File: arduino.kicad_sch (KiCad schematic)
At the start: 10 parts, among them J10 Conn_01x01_Female, J11 Conn_01x03_Male, J12 Conn_01x01_Female, J13 Conn_01x01_Female, J14 Conn_01x03_Male, J15 Conn_01x01_Female, J16 Conn_01x01_Female, J17 Conn_01x03_Male, J18 Conn_01x01_Female, U9 CD74HC4067SM

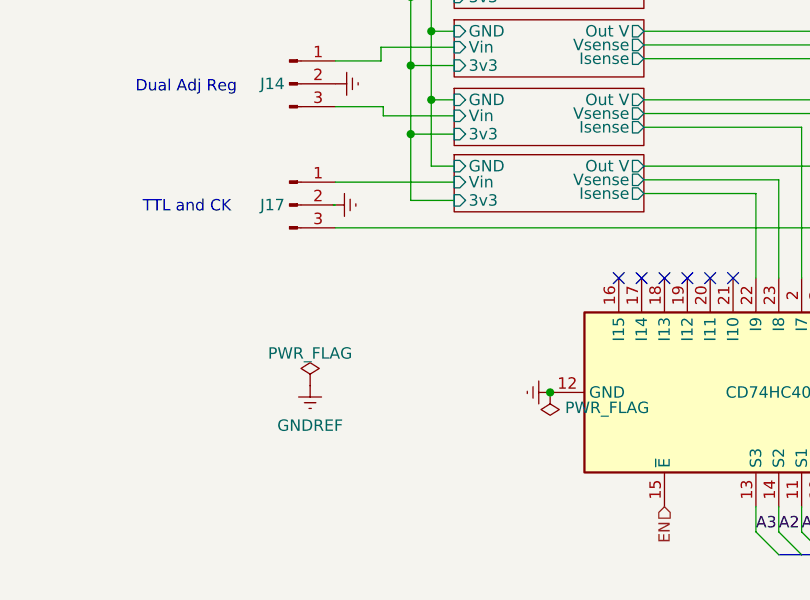
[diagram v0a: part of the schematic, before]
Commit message: sorting out earths and making measure mux board
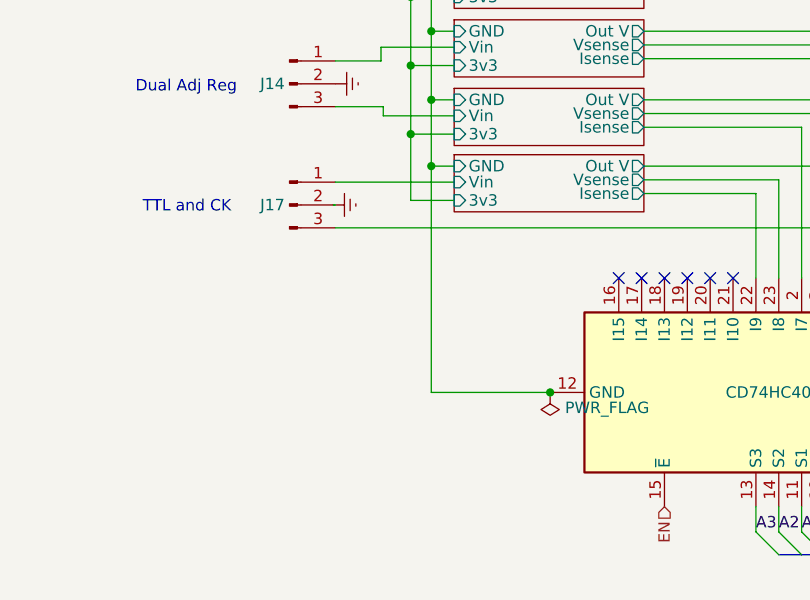
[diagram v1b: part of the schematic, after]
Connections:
- net Earth: no longer U9.12 (GND)
- net GND: now also U9.12 (GND)
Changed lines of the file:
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@@
   (junction (at 114.808 77.47) (diameter 0) (color 0 0 0 0)
   )
+  (junction (at 128.016 117.602) (diameter 0) (color 0 0 0 0)
+  )
   (junction (at 106.934 70.358) (diameter 0) (color 0 0 0 0)
   )
+  (junction (at 114.808 92.456) (diameter 0) (color 0 0 0 0)
+  )
   (junction (at 114.808 62.23) (diameter 0) (color 0 0 0 0)
   )
@@
   )
   (junction (at 112.522 81.28) (diameter 0) (color 0 0 0 0)
-  )
-  (junction (at 128.016 117.602) (diameter 0) (color 0 0 0 0)
   )
   (junction (at 108.966 64.008) (diameter 0) (color 0 0 0 0)
@@
     (stroke (width 0) (type default) (color 0 0 0 0))
   )
+  (wire (pts (xy 114.808 92.456) (xy 114.808 117.602))
+    (stroke (width 0) (type default) (color 0 0 0 0))
+  )
   (wire (pts (xy 138.43 80.518) (xy 161.036 80.518))
     (stroke (width 0) (type default) (color 0 0 0 0))
@@
   )
   (bus (pts (xy 158.496 135.636) (xy 161.036 135.636))
+    (stroke (width 0) (type default) (color 0 0 0 0))
+  )
+  (wire (pts (xy 114.808 117.602) (xy 128.016 117.602))
     (stroke (width 0) (type default) (color 0 0 0 0))
   )
@@
     (pin "1")
   )
-  (symbol (lib_id "power:GNDREF") (at 101.346 116.84 0) (unit 1)
-    (in_bom yes) (on_board yes) (fields_autoplaced)
-    (property "Reference" "#PWR0104" (id 0) (at 101.346 123.19 0)
-      (effects (font (size 1.27 1.27)) hide)
-    )
-    (property "Value" "GNDREF" (id 1) (at 101.346 121.2834 0))
-    (property "Footprint" "" (id 2) (at 101.346 116.84 0)
-      (effects (font (size 1.27 1.27)) hide)
-    )
-    (property "Datasheet" "" (id 3) (at 101.346 116.84 0)
-      (effects (font (size 1.27 1.27)) hide)
-    )
-    (pin "1")
-  )
   (symbol (lib_id "Connector:Conn_01x01_Female") (at 203.2 85.09 0) (unit 1)
     (in_bom yes) (on_board yes) (fields_autoplaced)
@@
     (pin "2")
     (pin "3")
-  )
-  (symbol (lib_id "power:PWR_FLAG") (at 101.346 116.84 0) (unit 1)
-    (in_bom yes) (on_board yes) (fields_autoplaced)
-    (property "Reference" "#FLG0117" (id 0) (at 101.346 114.935 0)
-      (effects (font (size 1.27 1.27)) hide)
-    )
-    (property "Value" "PWR_FLAG" (id 1) (at 101.346 113.2642 0))
-    (property "Footprint" "" (id 2) (at 101.346 116.84 0)
-      (effects (font (size 1.27 1.27)) hide)
-    )
-    (property "Datasheet" "~" (id 3) (at 101.346 116.84 0)
-      (effects (font (size 1.27 1.27)) hide)
-    )
-    (pin "1")
   )
   (symbol (lib_id "Connector:Conn_01x01_Female") (at 203.2 92.456 0) (unit 1)
@@
       (effects (font (size 1.27 1.27)) hide)
     )
-    (pin "1")
-  )
-  (symbol (lib_id "power:Earth") (at 128.016 117.602 270) (unit 1)
-    (in_bom no) (on_board yes) (fields_autoplaced)
-    (property "Reference" "#PWR07" (id 0) (at 121.666 117.602 0)
-      (effects (font (size 1.27 1.27)) hide)
-    )
-    (property "Value" "Earth" (id 1) (at 124.206 117.602 0)
-      (effects (font (size 1.27 1.27)) hide)
-    )
-    (property "Footprint" "" (id 2) (at 128.016 117.602 0)
-      (effects (font (size 1.27 1.27)) hide)
-    )
-    (property "Datasheet" "~" (id 3) (at 128.016 117.602 0)
-      (effects (font (size 1.27 1.27)) hide)
-    )

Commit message: last TH mounting board
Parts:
- added C10, C11, C12, C13, C14, C15, C16, C17: 0.1uF, Capacitor_SMD:C_0603_1608Metric, symbol Device:C_Small
- J1: renamed from J10; footprint (none) -> Connector_PinHeader_2.54mm:PinHeader_1x01_P2.54mm_Vertical
- J2: renamed from J11; footprint (none) -> Connector_PinHeader_2.54mm:PinHeader_1x03_P2.54mm_Horizontal
- J3: renamed from J12; footprint (none) -> Connector_PinHeader_2.54mm:PinHeader_1x01_P2.54mm_Vertical
- J4: renamed from J13; footprint (none) -> Connector_PinHeader_2.54mm:PinHeader_1x01_P2.54mm_Vertical
- J5: renamed from J14; footprint (none) -> Connector_PinHeader_2.54mm:PinHeader_1x03_P2.54mm_Horizontal
- J6: renamed from J15; footprint (none) -> Connector_PinHeader_2.54mm:PinHeader_1x01_P2.54mm_Vertical
- J7: renamed from J16; footprint (none) -> Connector_PinHeader_2.54mm:PinHeader_1x01_P2.54mm_Vertical
- J8: renamed from J17; footprint (none) -> Connector_PinHeader_2.54mm:PinHeader_1x03_P2.54mm_Horizontal
- J9: renamed from J18; footprint (none) -> Connector_PinHeader_2.54mm:PinHeader_1x01_P2.54mm_Vertical
- renumbered U9 to U4
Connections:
- net Earth is gone; now on net GND: J2.2 (Pin_2), J5.2 (Pin_2), J8.2 (Pin_2)
- net Curent and Volt4/Out V: now also C12.2
- net Curent and Volt5/Out V: now also C13.2
- net Curent and Volt5/Vsense: no longer U4.7 (I2)
- net Curent and Volt6/Out V: now also C14.2
- net Curent and Volt7/Out V: now also C15.2
- net Curent and Volt7/Vsense: no longer U4.3 (I6)
- net Curent and Volt8/Out V: now also C16.2
- net GND: now also C10.1, C11.1, C12.1, C13.1, C14.1, C15.1, C16.1, C17.1
- net Vunreg+: now also C11.2
- net Vunreg-: now also C10.2
- net at J8.3 (Pin_3), J9.1 (Pin_1): now also C17.2
- new net Unity Inverter/Ainv: U4.7 (I2)
- new net Unity Inverter1/Ainv: U4.3 (I6)
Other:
- added sheet Unity Inverter (UnityInverter.kicad_sch)
- added sheet Unity Inverter1 (UnityInverter.kicad_sch)
- moved on the sheet: J1, J3, J4, J6, J7, J9, U4

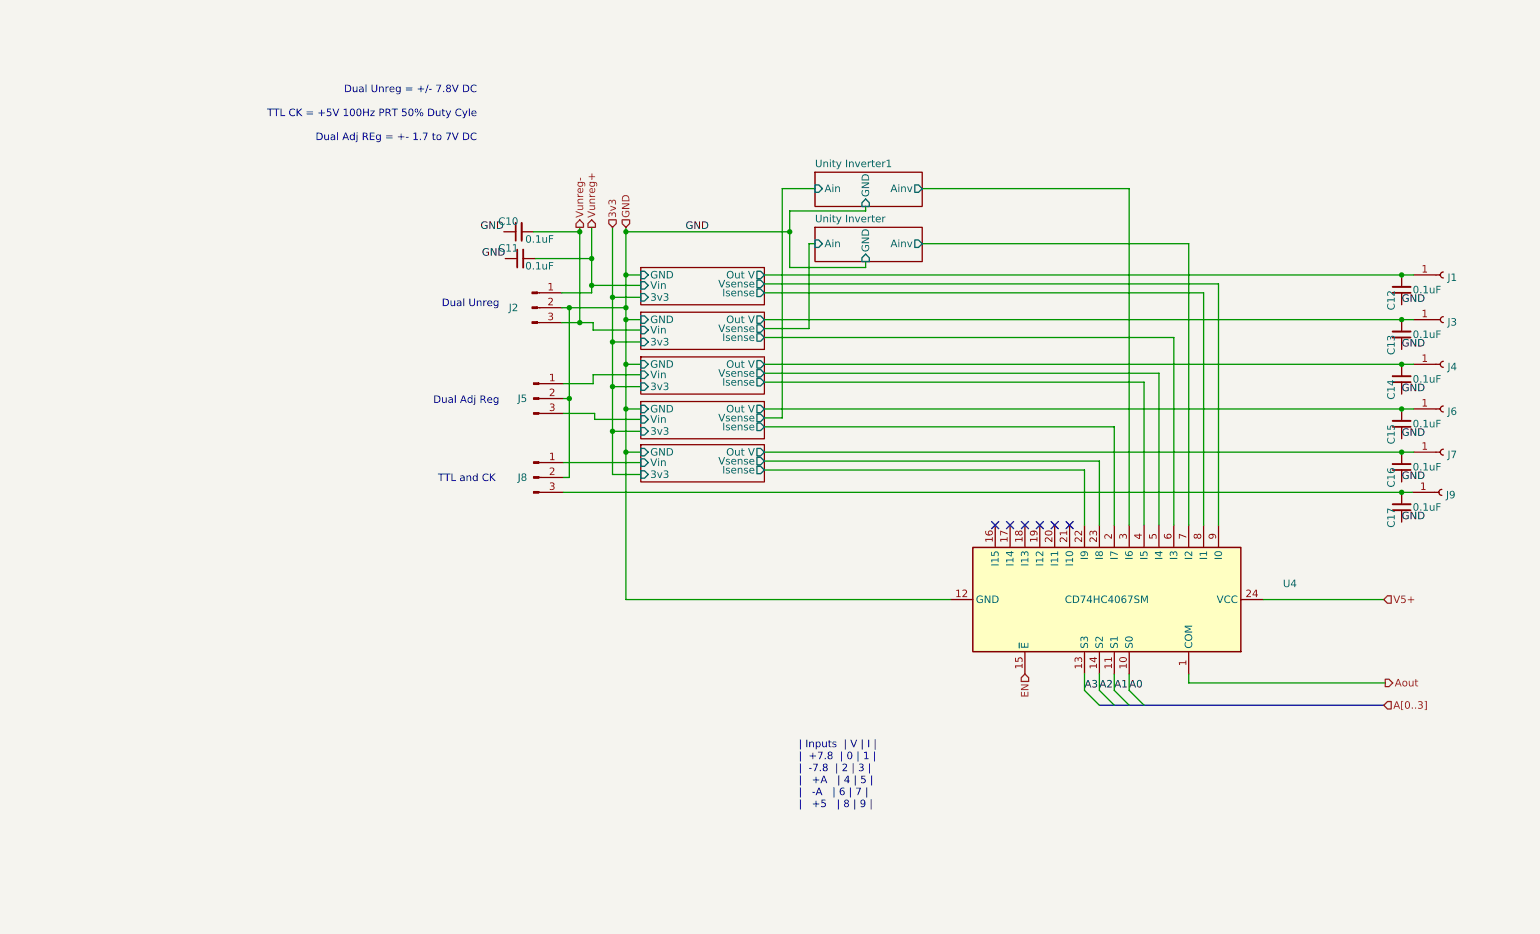
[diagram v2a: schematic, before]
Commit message: new board with SMD
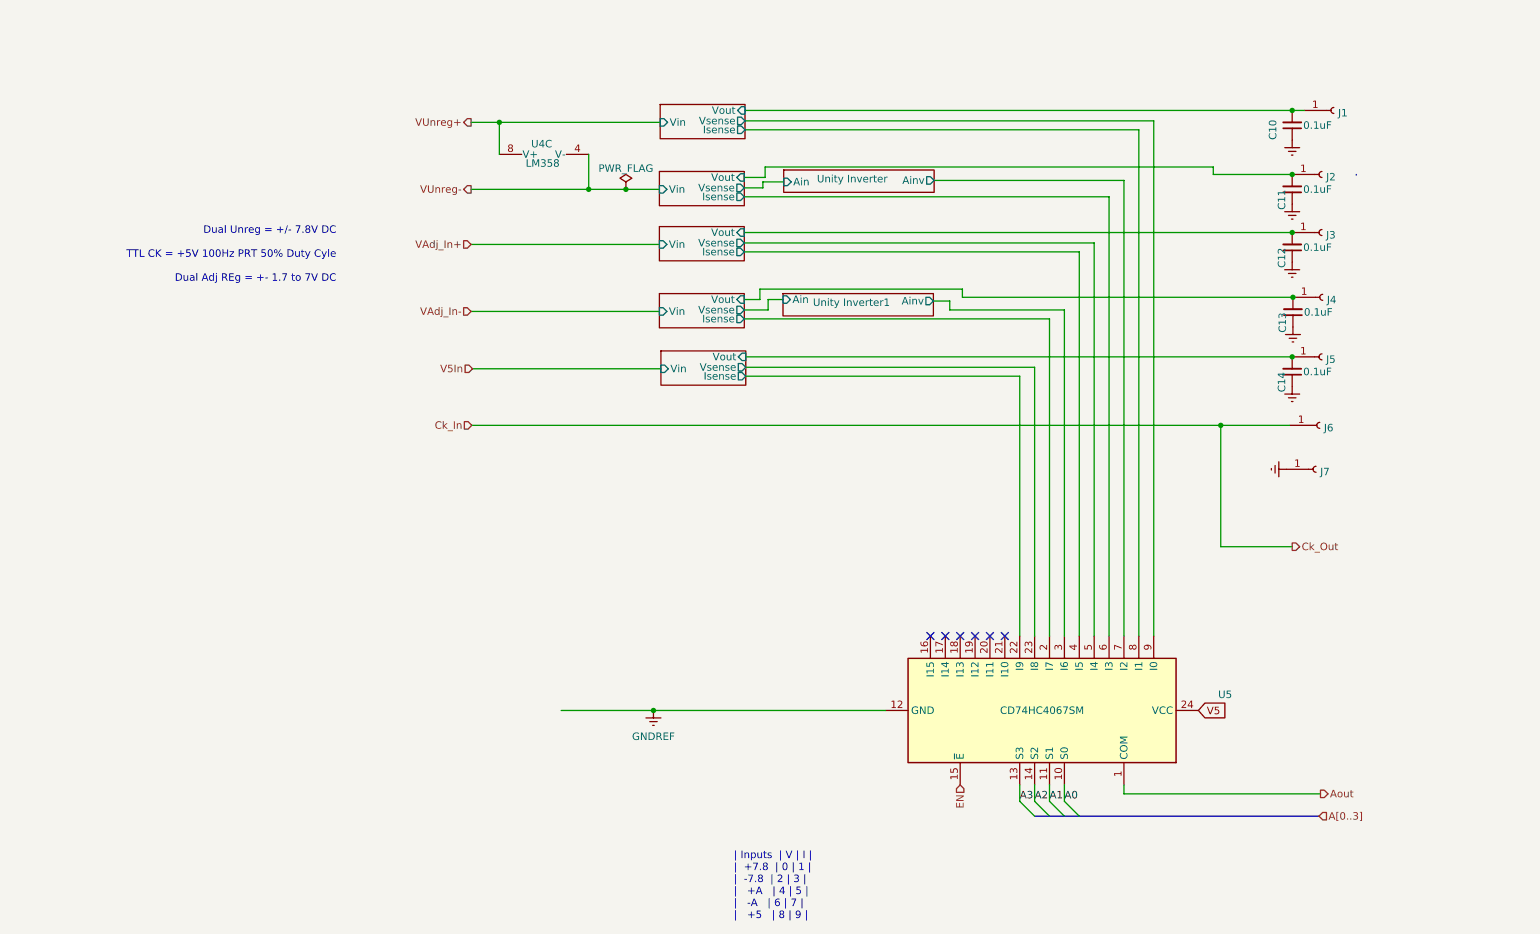
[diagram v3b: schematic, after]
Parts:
- removed C10, C11, C17: 0.1uF, Capacitor_SMD:C_0603_1608Metric, symbol Device:C_Small
- removed J2, J5, J8: Conn_01x03_Male, Connector_PinHeader_2.54mm:PinHeader_1x03_P2.54mm_Horizontal, symbol Connector:Conn_01x03_Male
- removed J9: Conn_01x01_Female, Connector_PinHeader_2.54mm:PinHeader_1x01_P2.54mm_Vertical, symbol Connector:Conn_01x01_Female
- added J6, J7: Conn_01x01_Female, Connector_PinHeader_2.54mm:PinHeader_1x01_P2.54mm_Vertical, symbol Connector:Conn_01x01_Female
- added U4: LM358, Package_TO_SOT_SMD:SOT-223-8, symbol Amplifier_Operational:LM358
- renumbered C12 to C10, C13 to C11, C14 to C12, C15 to C13, C16 to C14, J3 to J2, J4 to J3, J6 to J4, J7 to J5, U4 to U5
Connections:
- net Curent and Volt4/Out V renamed Curent and Volt4/Vout
- net Curent and Volt5/Out V renamed Curent and Volt5/Vout
- net Curent and Volt6/Out V renamed Curent and Volt6/Vout
- net Curent and Volt7/Out V renamed Curent and Volt7/Vout
- net Curent and Volt8/Out V renamed Curent and Volt8/Vout
- net GND renamed GNDREF
- net GNDREF: now also J7.1 (Pin_1)
- net V5+ renamed V5
- new net Ck_In: J6.1 (Pin_1)
- new net VUnreg+: U4.8 (V+)
- new net VUnreg-: U4.4 (V-)
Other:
- sheet Curent and Volt4 ports: added Vout; removed 3v3, GND, Out V
- sheet Curent and Volt5 ports: added Vout; removed 3v3, GND, Out V
- sheet Curent and Volt6 ports: added Vout; removed 3v3, GND, Out V
- sheet Curent and Volt7 ports: added Vout; removed 3v3, GND, Out V
- sheet Curent and Volt8 ports: added Vout; removed 3v3, GND, Out V
- sheet Unity Inverter ports: added none; removed GND
- sheet Unity Inverter1 ports: added none; removed GND
- note removed: "Dual Adj Reg"
- note removed: "Dual Unreg"
- note removed: "TTL and CK"
- moved on the sheet: C10, C11, C12, C13, C14, J1, J2, J3, J4, J5, U5

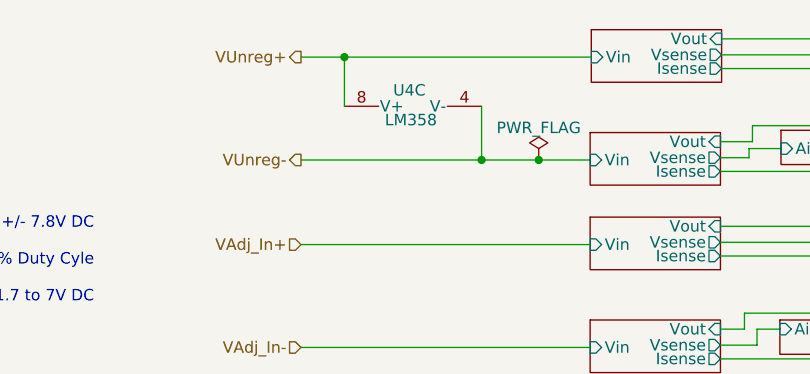
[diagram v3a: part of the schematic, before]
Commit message: New single board with all SMD in progress
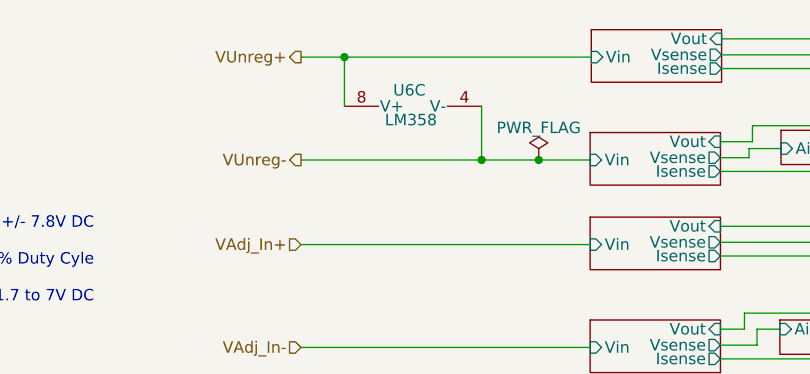
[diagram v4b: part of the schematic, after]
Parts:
- renumbered U4 to U6
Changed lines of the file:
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@@
   (symbol (lib_id "Amplifier_Operational:LM358") (at 100.838 39.116 90) (unit 3)
     (in_bom yes) (on_board yes)
-    (property "Reference" "U4" (id 0) (at 102.235 39.878 90)
+    (property "Reference" "U6" (id 0) (at 102.235 39.878 90)
       (effects (font (size 1.27 1.27)) (justify left))
     )
